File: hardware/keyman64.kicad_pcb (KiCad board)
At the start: 2 copper layers, 80 x 59.7 mm, 28 parts, among them IC1 ATMEGA1284P-P, P1 TAPEPORT, P2 CIA1, P3 KEYBOARD, P4 USER, P6 USB, SW1 RESET, SW2 BOOTLOADER, U1 7400, U2 ICL7660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

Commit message: Hardware/Firmware: Swapped Cassette Sense and Data lines
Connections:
- IC1 pad 19: /CS -> /CD
- IC1 pad 20: /CD -> /CS
- P1 pad 1: /CS -> /CD
- P1 pad 2: /CD -> /CS
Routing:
- net /CS: track 12.4 -> 8.79 mm
- net /CD: track 8.79 -> 12.4 mm
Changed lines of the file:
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@@
-(kicad_pcb (version 3) (host pcbnew "(2013-07-07 BZR 4022)-stable")
+(kicad_pcb (version 3) (host pcbnew "(2013-may-18)-stable")
   (general
     (links 141)
-    (no_connects 0)
-    (area 168.555999 107.614601 269.759101 179.754201)
+    (no_connects 2)
+    (area 104.509899 57.436901 205.713001 129.576501)
     (thickness 1.6)
     (drawings 18)
@@
     (pad 1 thru_hole rect (at -1.27 0 180) (size 1.524 1.524) (drill 1.016)
       (layers *.Cu *.Mask F.SilkS)
+      (net 25 /CD)
+    )
+    (pad 2 thru_hole circle (at 1.27 0 180) (size 1.524 1.524) (drill 1.016)
+      (layers *.Cu *.Mask F.SilkS)
       (net 34 /CS)
-    )
-    (pad 2 thru_hole circle (at 1.27 0 180) (size 1.524 1.524) (drill 1.016)
-      (layers *.Cu *.Mask F.SilkS)
-      (net 25 /CD)
     )
     (model pin_array/pins_array_2x1.wrl
@@
     (pad 19 thru_hole circle (at 21.59 7.62 270) (size 1.397 1.397) (drill 0.8128)
       (layers *.Cu *.Mask F.SilkS)
+      (net 25 /CD)
+    )
+    (pad 20 thru_hole circle (at 24.13 7.62 270) (size 1.397 1.397) (drill 0.8128)
+      (layers *.Cu *.Mask F.SilkS)
       (net 34 /CS)
-    )
-    (pad 20 thru_hole circle (at 24.13 7.62 270) (size 1.397 1.397) (drill 0.8128)
-      (layers *.Cu *.Mask F.SilkS)
-      (net 25 /CD)
     )
     (pad 21 thru_hole circle (at 24.13 -7.62 270) (size 1.397 1.397) (drill 0.8128)
@@
   (segment (start 176.3364 73.4345) (end 176.3364 71.8904) (width 0.254) (layer B.Cu) (net 24))
   (segment (start 170.2181 79.5528) (end 176.3364 73.4345) (width 0.254) (layer B.Cu) (net 24))
-  (segment (start 141.3129 120.1039) (end 146.8247 125.6157) (width 0.254) (layer B.Cu) (net 25))
-  (segment (start 140.3223 120.1039) (end 141.3129 120.1039) (width 0.254) (layer B.Cu) (net 25))
+  (segment (start 140.3223 117.5639) (end 141.3129 117.5639) (width 0.254) (layer B.Cu) (net 25))
+  (segment (start 141.3129 117.5639) (end 149.3647 125.6157) (width 0.254) (layer B.Cu) (net 25))
   (segment (start 140.8557 70.6247) (end 141.3637 70.6247) (width 0.254) (layer B.Cu) (net 26))
   (segment (start 153.923998 72.644002) (end 154.7241 71.8439) (width 0.254) (layer B.Cu) (net 26))
@@
   (via (at 159.9259 92.0364) (size 0.889) (layers F.Cu B.Cu) (net 33))
   (segment (start 160.80455 91.15775) (end 159.9259 92.0364) (width 0.254) (layer F.Cu) (net 33))
-  (segment (start 140.3223 117.5639) (end 141.3129 117.5639) (width 0.254) (layer B.Cu) (net 34))
-  (segment (start 141.3129 117.5639) (end 149.3647 125.6157) (width 0.254) (layer B.Cu) (net 34))
+  (segment (start 141.3129 120.1039) (end 146.8247 125.6157) (width 0.254) (layer B.Cu) (net 34))
+  (segment (start 140.3223 120.1039) (end 141.3129 120.1039) (width 0.254) (layer B.Cu) (net 34))
   (via (at 173.105 96.8313) (size 0.889) (layers F.Cu B.Cu) (net 35))
   (segment (start 173.105 96.9475) (end 173.105 96.8313) (width 0.254) (layer F.Cu) (net 35))

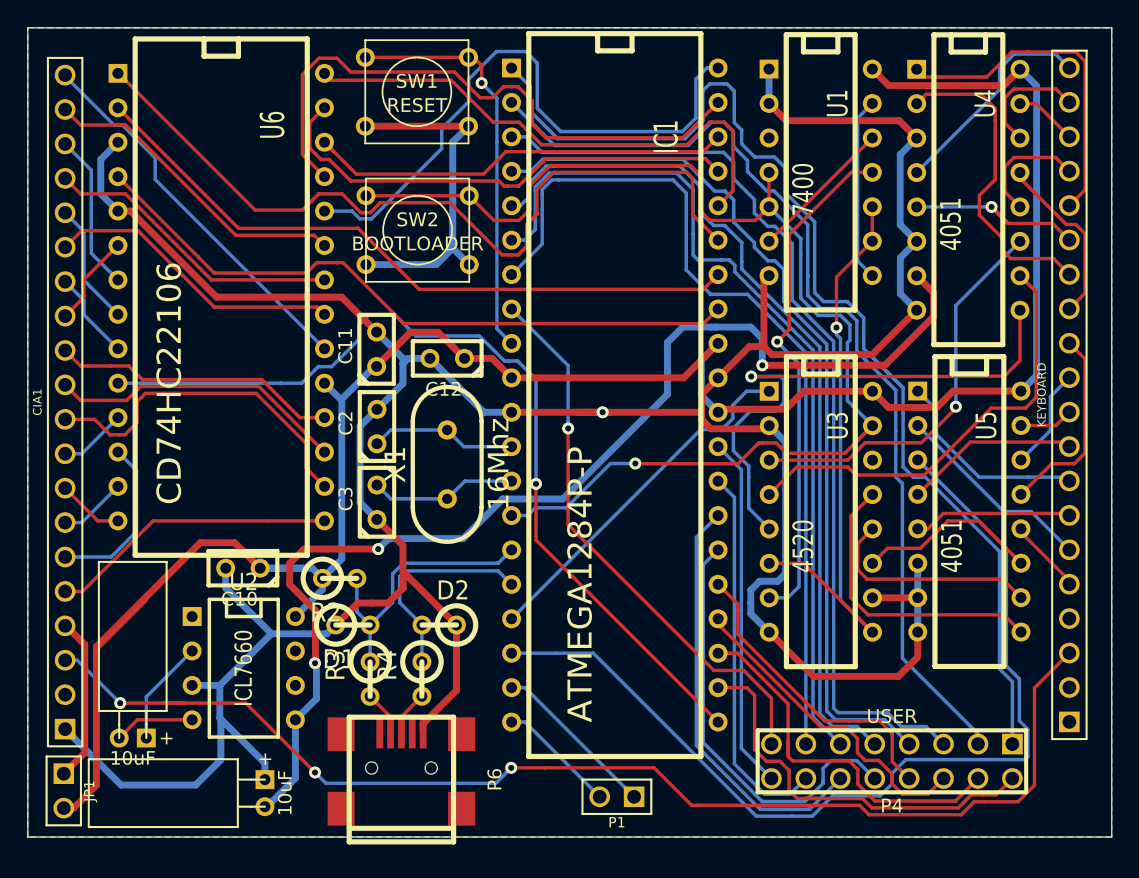
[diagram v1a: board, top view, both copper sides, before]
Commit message: Hardware: Fixed bug in schematics/pcb (4520 enable to VCC)
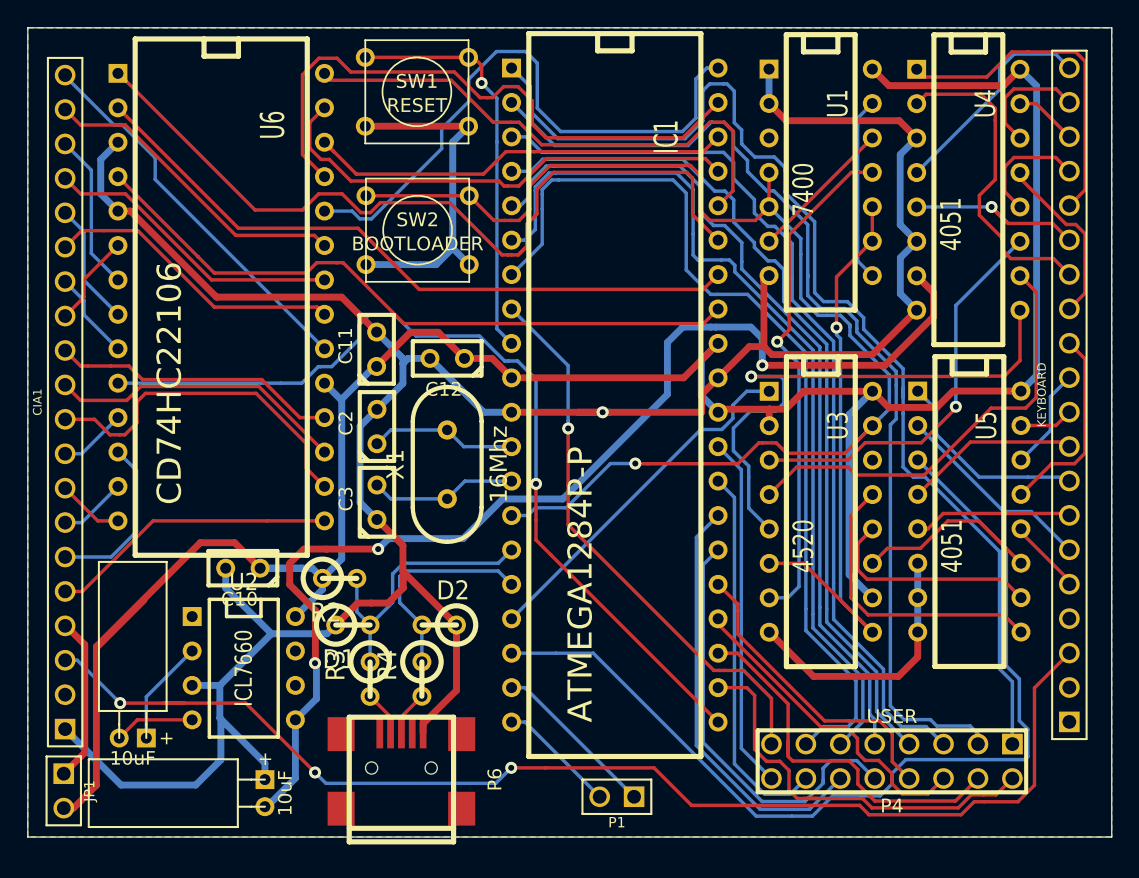
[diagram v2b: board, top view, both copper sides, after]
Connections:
- P2 pad 2: (no net) -> N-0000067
- P3 pad 2: (no net) -> N-0000066
- P3 pad 4: (no net) -> N-0000041
- P6 pad 1: (no net) -> N-0000032
- P6 pad 4: (no net) -> N-0000034
- P6 pad 6: (no net) -> N-0000035
- P6 pad 7: (no net) -> N-0000036
- P6 pad 8: (no net) -> N-0000037
- P6 pad 9: (no net) -> N-0000038
- U1 pad 3: (no net) -> N-0000040
- U2 pad 6: (no net) -> N-0000028
- U2 pad 7: (no net) -> N-0000026
- U3 pad 10: GND -> VCC
- U3 pad 14: (no net) -> N-0000094
- U3 pad 2: GND -> VCC
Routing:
- net GND: track 269.9 -> 242.5 mm
- net VCC: track 162.1 -> 180.1 mm
- net /UA6: track 64.5 -> 68.6 mm
- net /UA1: track 72.8 -> 75.8 mm
- net /UA0: track 86.1 -> 83.8 mm
- net /UA3: track 66.0 -> 63.8 mm
- net /UA2: track 70.0 -> 67.9 mm
- net /UA5: track 64.6 -> 66.0 mm
- net /UA4: track 64.4 -> 63.3 mm
- net /MR: track 91.6 -> 92.5 mm

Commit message: Hardware: Removed EXTVCC Jumper, removed copper around edges
There is no VCC on the keyboard connector, so VCC must be fed from external
source anyways if the keyboard cable is simply cut in half and the board
soldered in between.

The copper/traces around the keyboard/cia connectors have been removed to
make it easier to simply solder the wires in instead of adding pin headers
and proper plugs.
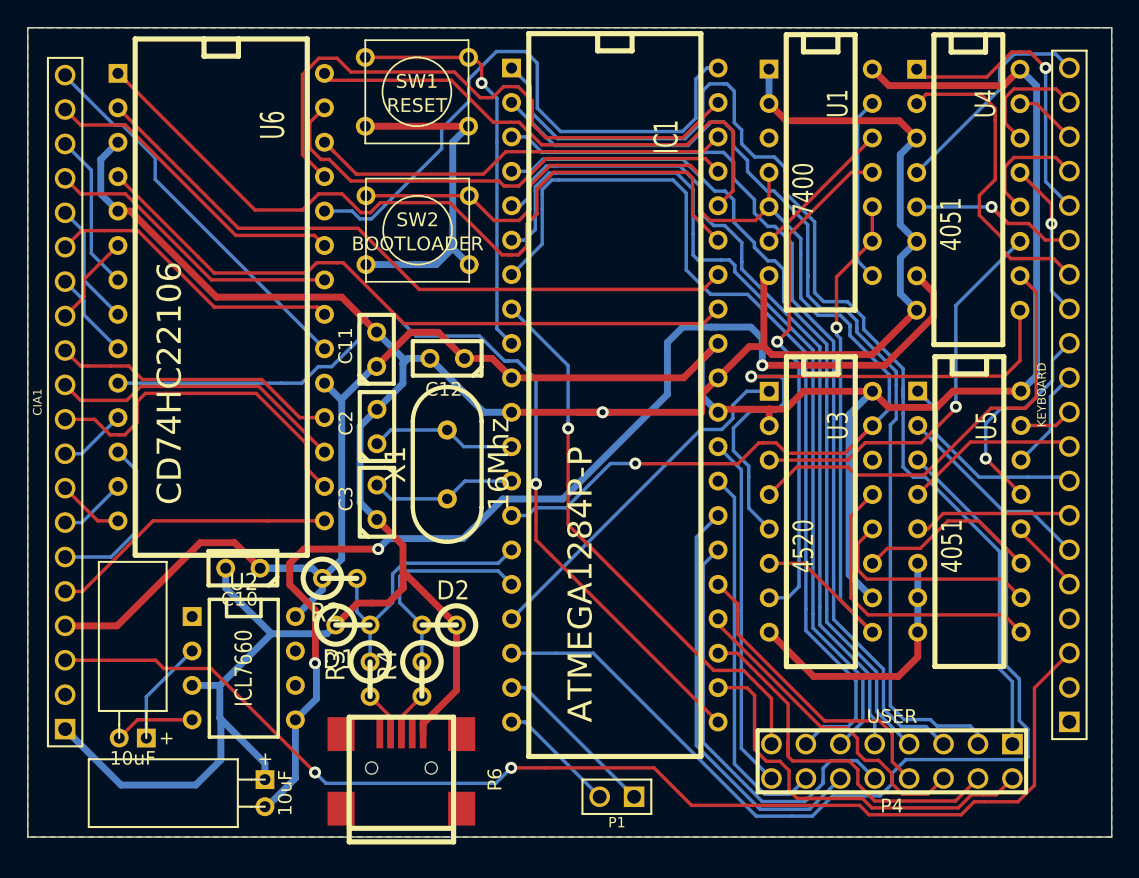
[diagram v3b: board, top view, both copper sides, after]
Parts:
- removed JP1: JUMPER, PIN_ARRAY_2X1
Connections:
- P2 pad 2: N-0000067 -> (no net)
- P2 pad 4: /EXTVCC -> VCC
- P3 pad 2: N-0000066 -> (no net)
- P3 pad 4: N-0000041 -> (no net)
- P6 pad 1: N-0000032 -> (no net)
- P6 pad 4: N-0000034 -> (no net)
- P6 pad 6: N-0000035 -> (no net)
- P6 pad 7: N-0000036 (its old number) -> (no net)
- P6 pad 8: N-0000037 -> (no net)
- P6 pad 9: N-0000038 -> (no net)
- U1 pad 3: N-0000040 -> (no net)
- U2 pad 6: N-0000028 (its old number) -> (no net)
- U2 pad 7: N-0000026 -> (no net)
- U3 pad 14: N-0000094 -> (no net)
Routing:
- net VCC: track 180.1 -> 162.0 mm
- net /EXTVCC: track 12.2 -> 0.00 mm
- net /C4: track 24.8 -> 21.9 mm, vias 0 -> 1
- net /C0: track 12.9 -> 11.6 mm, vias 0 -> 1
- net /R0: track 14.6 -> 15.8 mm, vias 0 -> 1
- net /~RESTORE: track 90.5 -> 89.8 mm, vias 3 -> 2

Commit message: Hardware: Improved routing around the edge connectors
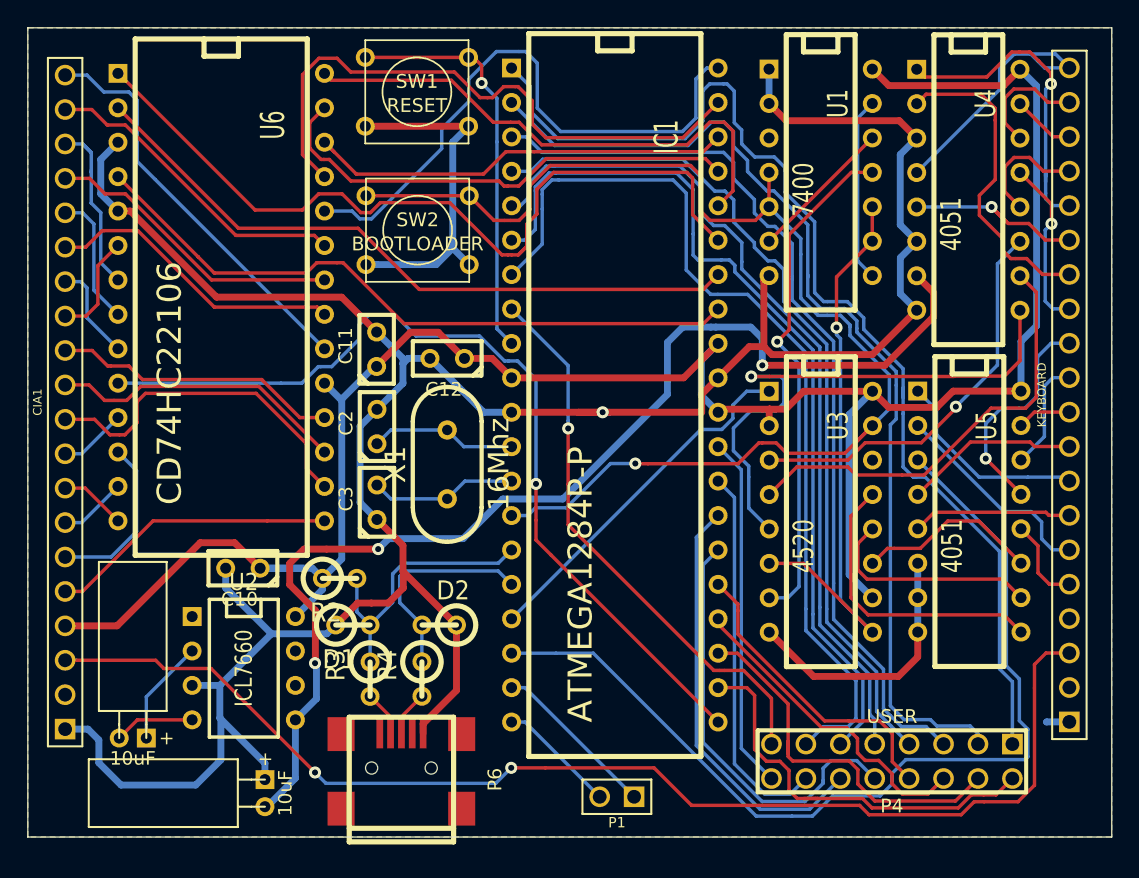
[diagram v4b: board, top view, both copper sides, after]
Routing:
- net /C7: track 16.2 -> 19.5 mm
- net GND: track 242.5 -> 245.2 mm
- net /C4: track 21.9 -> 23.8 mm
- net /A2: track 11.6 -> 13.5 mm
- net /A7: track 28.5 -> 30.2 mm
- net /R3: track 5.83 -> 6.95 mm
- net /C0: track 11.6 -> 12.7 mm
- net /~RESTORE: track 89.8 -> 90.8 mm
- net /A0: track 6.82 -> 7.72 mm
- net /R0: track 15.8 -> 16.6 mm
- net /A4: track 9.11 -> 9.87 mm
- net /R6: track 15.0 -> 15.7 mm
- net /R1: track 7.55 -> 8.26 mm
- net /A6: track 6.57 -> 7.24 mm

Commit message: Hardware: Moved values and refs on pcb, added svg renderings
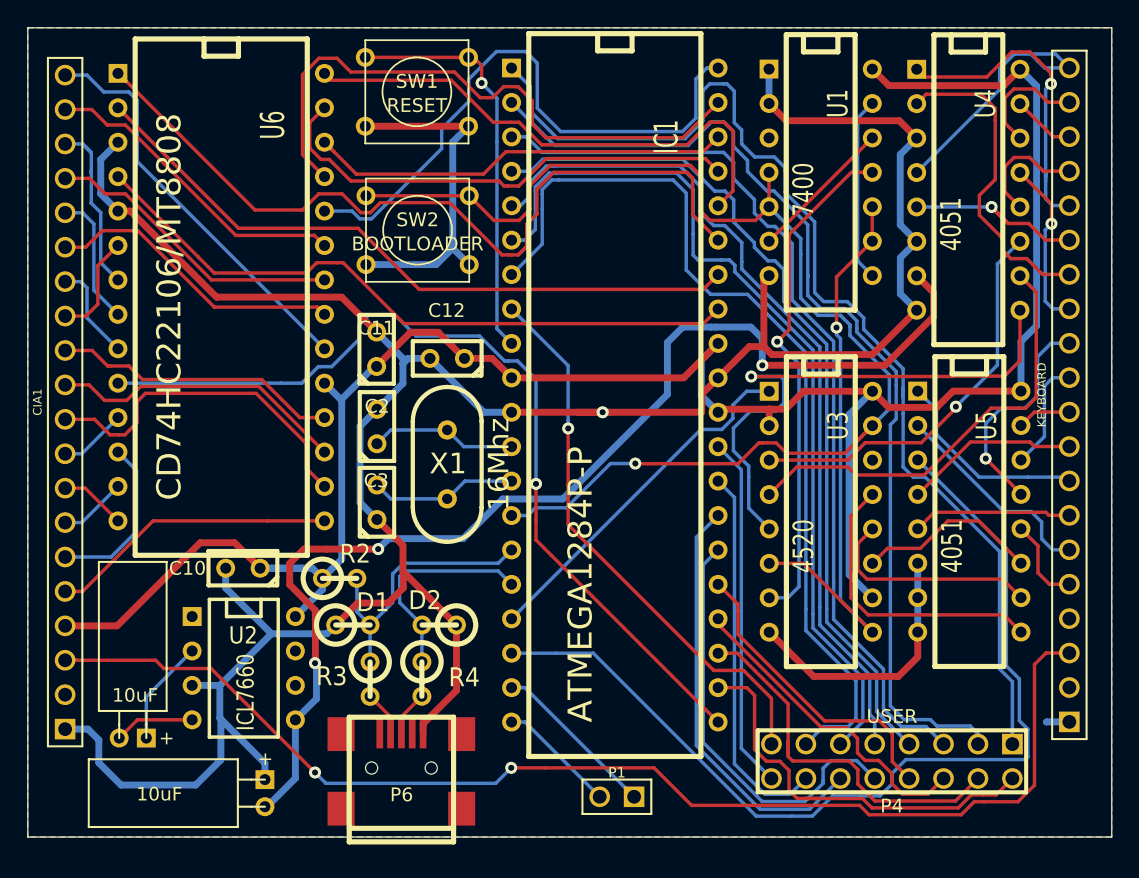
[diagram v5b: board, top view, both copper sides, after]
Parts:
- P1: value TAPEPORT -> SERIAL
- U6: value CD74HC22106 -> CD74HC22106/MT8808

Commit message: Hardware: Rev.2, Increased VIA sizes, Added alternative VCC pin header
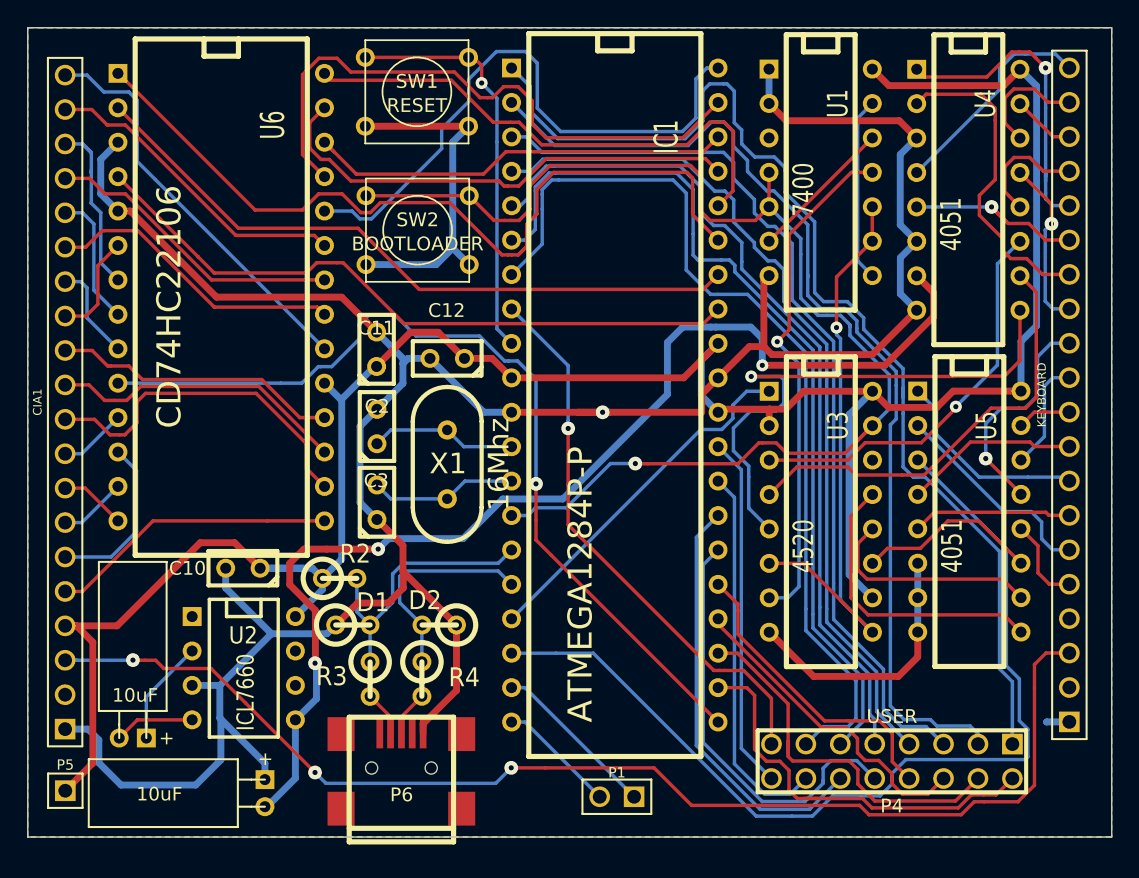
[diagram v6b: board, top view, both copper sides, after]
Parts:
- added P5: POWER, PIN_ARRAY_1, F.Cu at (107.4, 125.2)
- U6: value CD74HC22106/MT8808 -> CD74HC22106
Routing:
- net VCC: track 162.0 -> 176.4 mm
- net /C7: track 19.5 -> 16.2 mm
- net /~RESTORE: vias 2 -> 3
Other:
- net class Default: via_dia 0.889 -> 1.016; via_drill 0.635 -> 0.381
- net class Power: via_dia 0.889 -> 1.016; via_drill 0.635 -> 0.381
- rule via_min_drill: 0.508 -> 0.381
